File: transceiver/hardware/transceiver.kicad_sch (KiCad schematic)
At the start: 54 parts, among them J1 Conn_Coaxial, J2 Conn_Coaxial, J3 Conn_01x04, J4 Conn_01x02, U1 STM32L431KCUx, U2 LR2021, Y1 32.768KHz, Y3 32MHz 10pF

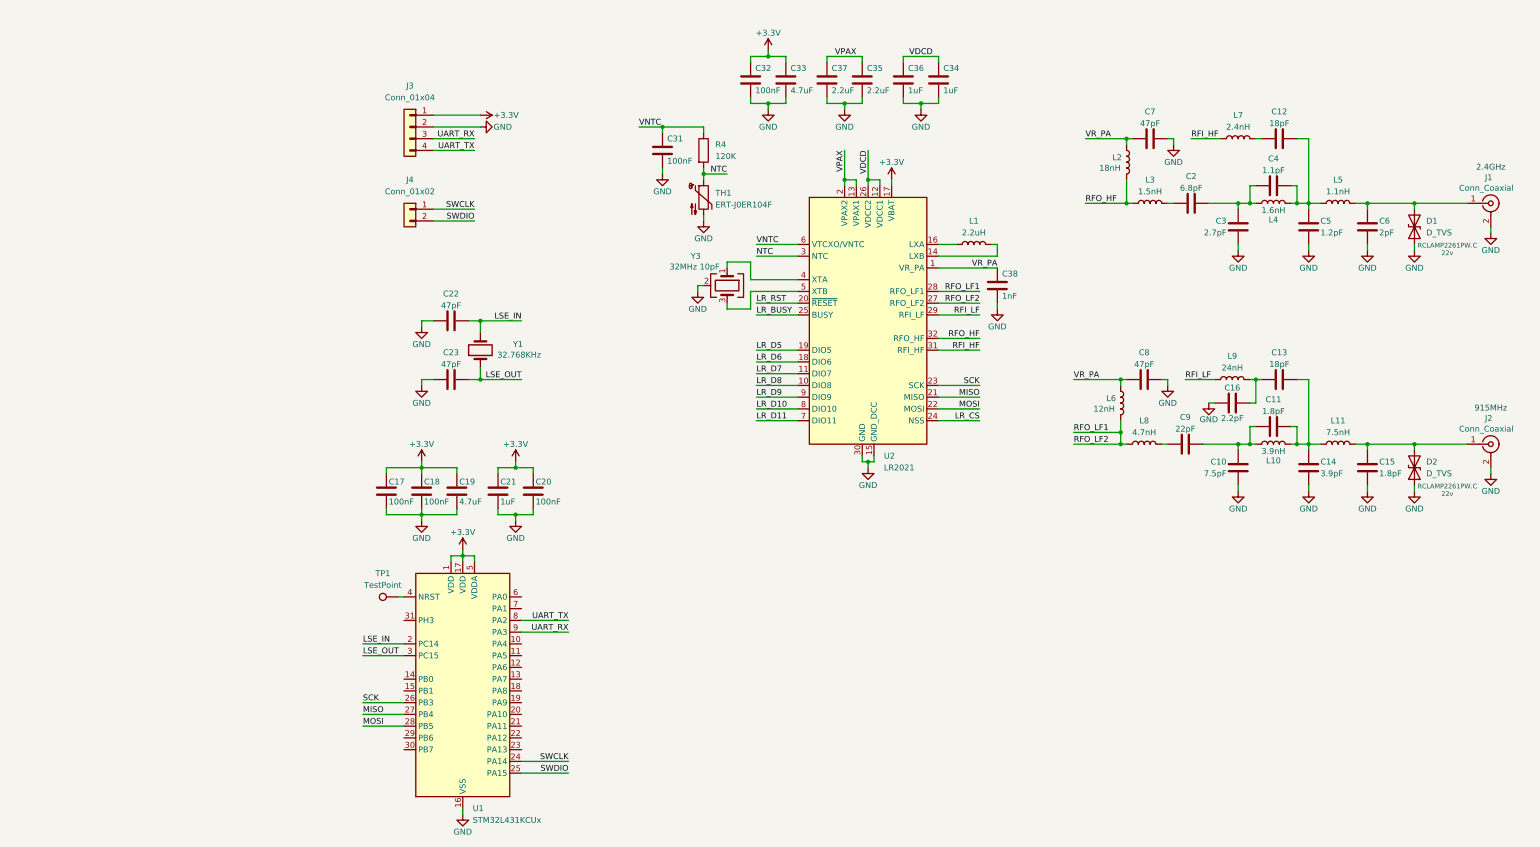
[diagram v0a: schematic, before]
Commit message: added mcu and gps
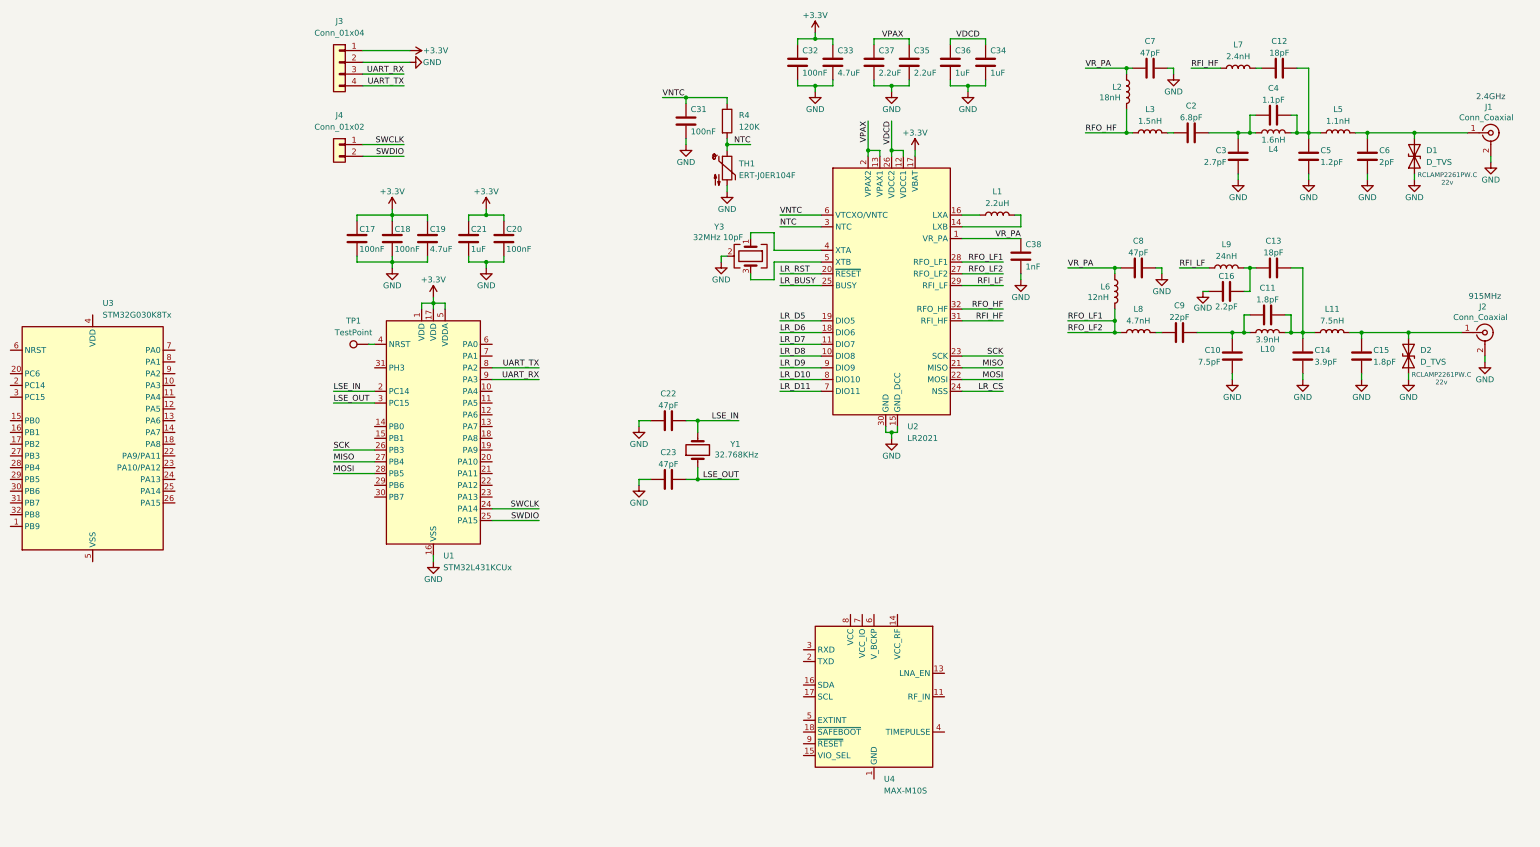
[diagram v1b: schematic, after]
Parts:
- added U3: STM32G030K8Tx, Package_QFP:LQFP-32_7x7mm_P0.8mm, symbol MCU_ST_STM32G0:STM32G030K8Tx
- added U4: MAX-M10S, RF_GPS:ublox_MAX, symbol RF_GPS:MAX-M10S
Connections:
- new net: U4.1 (GND), U4.10 (GND), U4.12 (GND)
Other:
- moved on the sheet: C10, C11, C12, C13, C14, C15, C16, C17, C18, C19, C2, C20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

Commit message: changed mcu and added gps
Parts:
- removed C20: 100nF, Capacitor_SMD:C_0402_1005Metric, symbol Device:C
- removed C21: 1uF, Capacitor_SMD:C_0402_1005Metric, symbol Device:C
- removed U1: STM32L431KCUx, Package_DFN_QFN:QFN-32-1EP_5x5mm_P0.5mm_EP3.45x3.45mm, symbol MCU_ST_STM32L4:STM32L431KCUx
- added BT1: MS621FE-FL11E, Flight-Controller_Imports:BAT_MS621FE-FL11E, symbol Device:Battery_Cell
- added D3: D_Schottky, Diode_SMD:D_0603_1608Metric, symbol Device:D_Schottky
- added J5: Conn_Coaxial, Connector_Coaxial:U.FL_Molex_MCRF_73412-0110_Vertical, symbol Connector:Conn_Coaxial
- added R3: 1K, Resistor_SMD:R_0402_1005Metric, symbol Device:R
- added TP2: TestPoint, TestPoint:TestPoint_Pad_D1.0mm, symbol Connector:TestPoint
- C17: value 100nF -> 1uF; footprint Capacitor_SMD:C_0402_1005Metric -> Capacitor_SMD:C_0603_1608Metric
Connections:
- net LR_CS is gone; now on net NSS: U2.24 (NSS)
- net +3.3V: now also U3.4 (VDD), U4.7 (VCC_IO), U4.8 (VCC), D3.2 (A); no longer C17.1
- net GND: now also U3.5 (VSS), U4.1 (GND), U4.10 (GND), U4.12 (GND), BT1.2 (-), J5.2 (Ext)
- net LSE_IN: now also U3.2 (PC14)
- net LSE_OUT: now also U3.3 (PC15)
- net MISO: now also U3.13 (PA6)
- net MOSI: now also U3.14 (PA7)
- net SCK: now also U3.12 (PA5)
- net SWCLK: now also U3.25 (PA14)
- net SWDIO: now also U3.24 (PA13)
- net UART_RX: now also U3.10 (PA3)
- net UART_TX: now also U3.9 (PA2)
- net NSS: now reaches U3.11 (PA4)
- net at U3.6 (NRST): now also TP1.1
- net at U4.11 (RF_IN): now also J5.1 (In)
- net at U4.18 (~{SAFEBOOT}): now also TP2.1
- net GPS_RX: now reaches U4.2 (TXD)
- net GPS_TX: now reaches U4.3 (RXD)
- net GPS_LED: now reaches U4.4 (TIMEPULSE)
- net GPS_INT: now reaches U4.5 (EXTINT)
- net V_BCKP: now reaches U4.6 (V_BCKP)
- net V_BCKP: now also C17.1, BT1.1 (+), R3.2
- net GPS_RESET: now reaches U4.9 (~{RESET})
- new net: D3.1 (K), R3.1
- no-connect marks 0 -> 5
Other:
- moved on the sheet: C18, C19, C22, C23, TP1, U3, U4, Y1
